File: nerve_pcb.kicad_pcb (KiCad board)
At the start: 6 copper layers, 50 x 50 mm, 76 parts, among them J1 TC2050-IDC, J2 2171750001, J4 472192001, J5 BF030-16A-B1-0360-0277-0600-LB, J6 BF080-20-A-1-L-C, J7 UART, J8 CAN1, J9 CAN2, SW1 SPST, SW2 SPST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

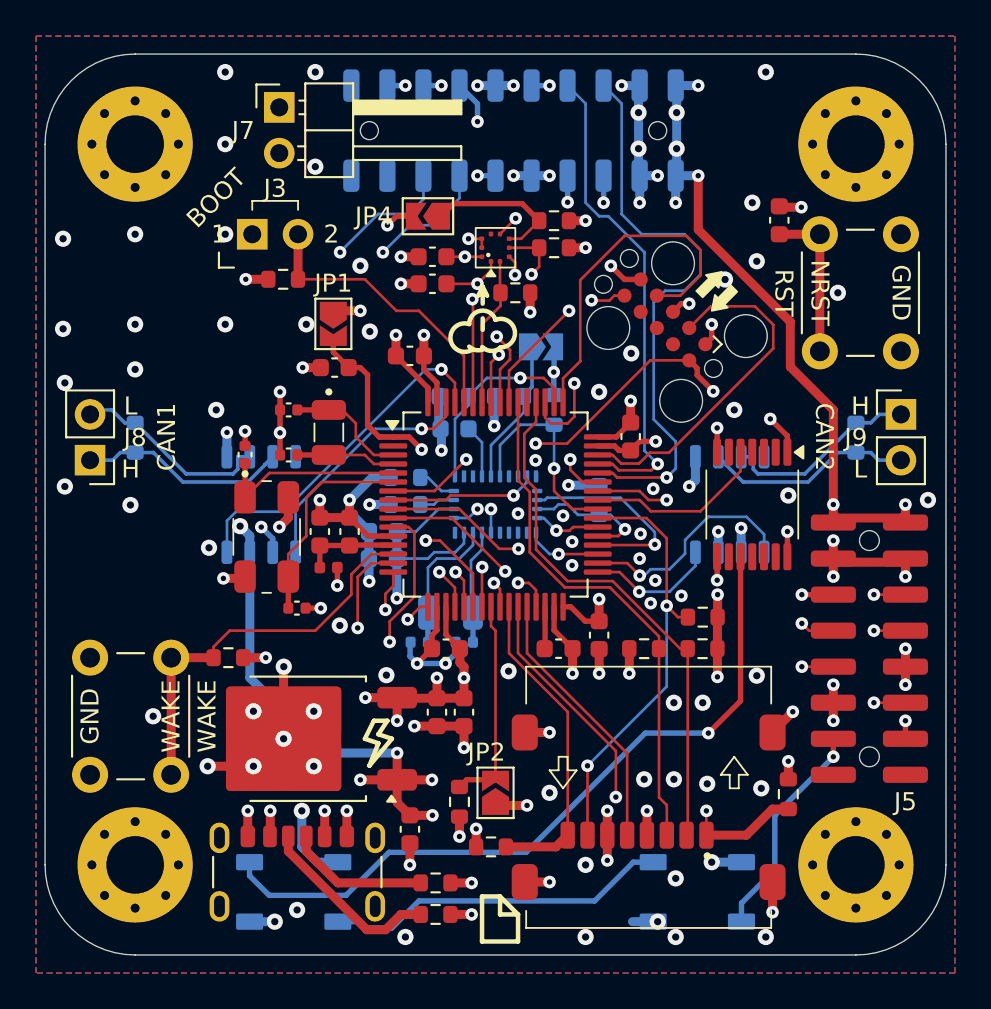
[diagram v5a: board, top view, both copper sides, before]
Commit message: Cleanup and add fiducials
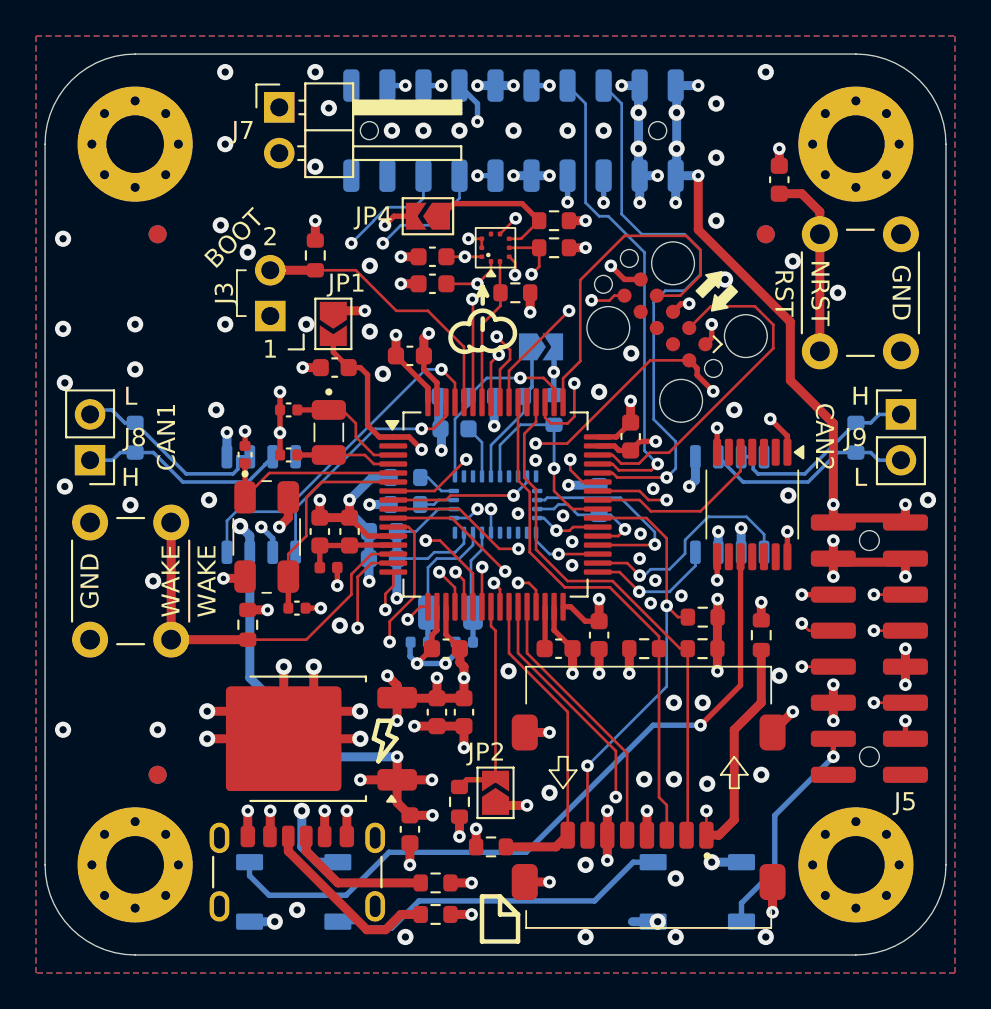
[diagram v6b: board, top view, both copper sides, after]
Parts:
- added FM1: 1mm, Fiducial:Fiducial_1mm_Mask2mm, F.Cu at (129.8, 120.0)
- added FM2: 1mm, Fiducial:Fiducial_1mm_Mask2mm, F.Cu at (129.8, 90.0)
- added FM3: 1mm, Fiducial:Fiducial_1mm_Mask2mm, F.Cu at (163.5, 90.0)
- added FM4: 1mm, Fiducial:Fiducial_1mm_Mask2mm, B.Cu at (129.8, 120.0)
- added FM5: 1mm, Fiducial:Fiducial_1mm_Mask2mm, B.Cu at (129.8, 90.0)
- added FM6: 1mm, Fiducial:Fiducial_1mm_Mask2mm, B.Cu at (163.5, 90.0)
- moved R8 8.95 mm to (163.2, 112.2)
- moved SW2 7.50 mm to (130.5, 106.0)
- moved J3 3.28 mm to (136.0, 93.3), turned to 90 degrees
- moved C11 2.25 mm to (164.2, 87.0)
- moved R9 2.22 mm to (138.5, 91.2), turned to -90 degrees
- moved R3 2.12 mm to (134.8, 111.7), turned to -90 degrees
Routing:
- net GND: track 105.4 -> 118.8 mm, vias 122 -> 132
- net /SDIO_D2: track 24.8 -> 31.6 mm
- net /PA4: track 34.0 -> 31.8 mm
- net /NRST: track 37.2 -> 38.8 mm
- net /PA5: track 33.4 -> 32.1 mm
- net Net-(U2-PA0): track 22.2 -> 21.5 mm
- net +3V3: track 90.6 -> 90.0 mm
- net /PA7: track 32.9 -> 32.3 mm
- net /TIM1_CH1_PWM_{5V}: track 40.9 -> 40.4 mm

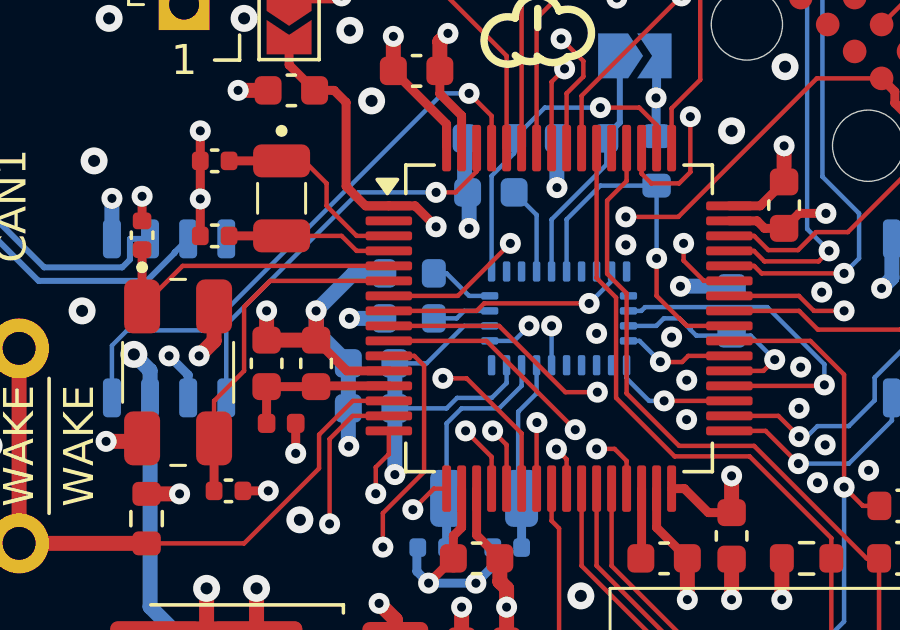
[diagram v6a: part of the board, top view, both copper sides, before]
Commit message: Fix BNO085 circuit for SPI
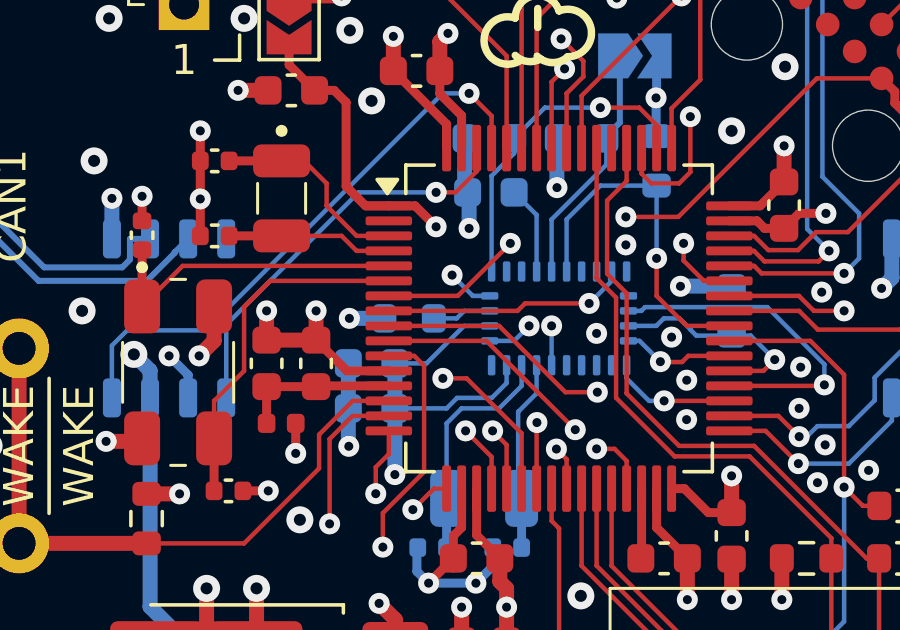
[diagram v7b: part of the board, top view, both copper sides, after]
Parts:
- removed the R16 at (143.5, 103.5)
- renumbered R17 to R16, R18 to R17, R19 to R18, R20 to R19, R21 to R20
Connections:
- U4 pad 5: Net-(U4-PS1) -> +3V3
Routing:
- net GND: track 118.8 -> 113.8 mm
- net Net-(U4-PS1): track 2.17 -> 0.00 mm
- net +3V3: track 90.0 -> 91.5 mm, vias 40 -> 41
